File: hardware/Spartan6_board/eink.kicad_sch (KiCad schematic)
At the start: 15 parts, among them J3 FH12-40S-0.5SH, J6 DF12NB(3.0)-30DS-0.5V(51), J7 DF12NB(3.0)-30DS-0.5V(51), U6 MT9700-N

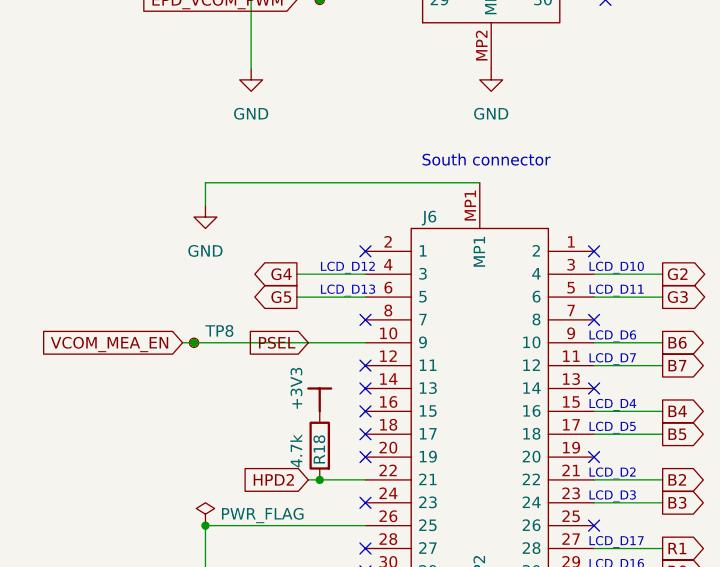
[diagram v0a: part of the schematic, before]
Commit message: fixed mixup of pins G5/G4 (3rd diff pair ODD) and DE/PCLK (3rd diff pair EVEN), now with correct polarity for diff pairs
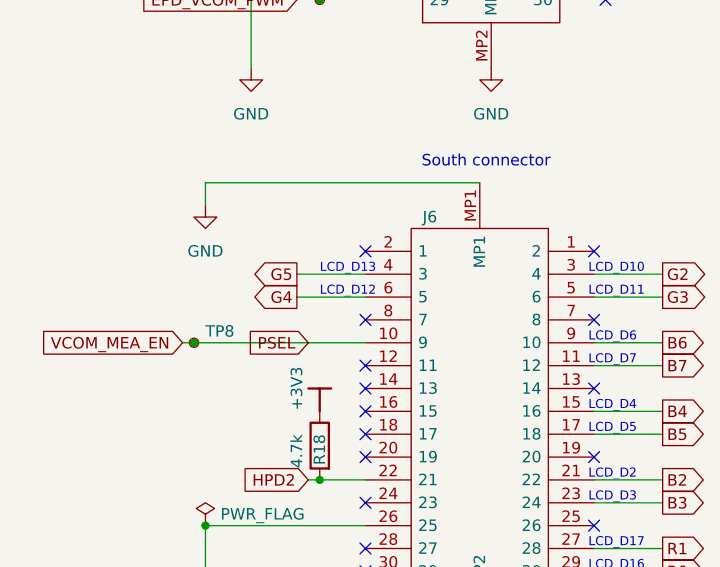
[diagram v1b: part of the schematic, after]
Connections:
- net G4: now also J6.6 (5); no longer J6.4 (3)
- net G5: now also J6.4 (3); no longer J6.6 (5)
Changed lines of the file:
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@@
+	(wire
+		(pts
+			(xy 31.75 142.24) (xy 39.37 142.24)
+		)
+		(stroke
+			(width 0.254)
+			(type default)
+		)
+	)
 	(wire
 		(pts
@@
 	(wire
 		(pts
+			(xy 129.54 118.11) (xy 129.54 119.38)
+		)
+		(stroke
+			(width 0)
+			(type default)
+		)
+	)
+	(wire
+		(pts
+			(xy 40.64 88.9) (xy 33.02 88.9)
+		)
+		(stroke
+			(width 0.254)
+			(type default)
+		)
+	)
+	(wire
+		(pts
+			(xy 33.02 91.44) (xy 40.64 91.44)
+		)
+		(stroke
+			(width 0.254)
+			(type default)
+		)
+	)
+	(wire
+		(pts
+			(xy 53.34 68.58) (xy 22.86 68.58)
+		)
+		(stroke
+			(width 0.254)
+			(type default)
+		)
+	)
+	(wire
+		(pts
+			(xy 119.38 151.13) (xy 119.38 153.67)
+		)
+		(stroke
+			(width 0)
+			(type default)
+		)
+	)
+	(wire
+		(pts
 			(xy 31.75 144.78) (xy 39.37 144.78)
 		)
@@
 	(wire
 		(pts
-			(xy 129.54 118.11) (xy 129.54 119.38)
-		)
-		(stroke
-			(width 0)
-			(type default)
-		)
-	)
-	(wire
-		(pts
-			(xy 40.64 88.9) (xy 33.02 88.9)
-		)
-		(stroke
-			(width 0.254)
-			(type default)
-		)
-	)
-	(wire
-		(pts
-			(xy 33.02 91.44) (xy 40.64 91.44)
-		)
-		(stroke
-			(width 0.254)
-			(type default)
-		)
-	)
-	(wire
-		(pts
-			(xy 53.34 68.58) (xy 22.86 68.58)
-		)
-		(stroke
-			(width 0.254)
-			(type default)
-		)
-	)
-	(wire
-		(pts
-			(xy 119.38 151.13) (xy 119.38 153.67)
-		)
-		(stroke
-			(width 0)
-			(type default)
-		)
-	)
-	(wire
-		(pts
 			(xy 107.95 140.97) (xy 109.22 140.97)
 		)
@@
 		(stroke
 			(width 0)
-			(type default)
-		)
-	)
-	(wire
-		(pts
-			(xy 31.75 142.24) (xy 39.37 142.24)
-		)
-		(stroke
-			(width 0.254)
 			(type default)
 		)
@@
 		)
 	)
-	(text "LCD_D13"
-		(exclude_from_sim no)
-		(at 34.29 144.78 0)
-		(effects
-			(font
-				(size 1 1)
-			)
-			(justify left bottom)
-		)
-	)
 	(text "LCD_D11"
 		(exclude_from_sim no)
@@
 		)
 	)
+	(text "LCD_D13"
+		(exclude_from_sim no)
+		(at 34.29 142.24 0)
+		(effects
+			(font
+				(size 1 1)
+			)
+			(justify left bottom)
+		)
+	)
 	(text "LCD_D18"
 		(exclude_from_sim no)
@@
 		)
 	)
-	(text "LCD_D12"
-		(exclude_from_sim no)
-		(at 34.29 142.24 0)
-		(effects
-			(font
-				(size 1 1)
-			)
-			(justify left bottom)
-		)
-	)
 	(text "LCD_D1"
 		(exclude_from_sim no)
@@
 		)
 	)
+	(text "LCD_D12"
+		(exclude_from_sim no)
+		(at 34.29 144.78 0)
+		(effects
+			(font
+				(size 1 1)
+			)
+			(justify left bottom)
+		)
+	)
 	(text "LCD_D9"
 		(exclude_from_sim no)
@@
 		)
 	)
+	(global_label "G5"
+		(shape output)
+		(at 31.75 142.24 180)
+		(fields_autoplaced yes)
+		(effects
+			(font
+				(size 1.27 1.27)
+			)
+			(justify right)
+		)
+		(property "Intersheetrefs" "${INTERSHEET_REFS}"
+			(at 26.2853 142.24 0)
+			(effects
+				(font
+					(size 1.27 1.27)
+				)
+				(justify right)
+				(hide yes)
+			)
+		)
+	)
 	(global_label "G1"
 		(shape output)
@@
 		(property "Intersheetrefs" "${INTERSHEET_REFS}"
 			(at 102.4853 120.65 0)
-			(effects
-				(font
-					(size 1.27 1.27)
-				)
-				(justify right)
-				(hide yes)
-			)
-		)
-	)
-	(global_label "G5"
-		(shape output)
-		(at 31.75 144.78 180)
-		(fields_autoplaced yes)
-		(effects
-			(font
-				(size 1.27 1.27)
-			)
-			(justify right)
-		)
-		(property "Intersheetrefs" "${INTERSHEET_REFS}"
-			(at 26.2853 144.78 0)
 			(effects
 				(font
@@
 		)
 	)
+	(global_label "G4"
+		(shape output)
+		(at 31.75 144.78 180)
+		(fields_autoplaced yes)
+		(effects
+			(font
+				(size 1.27 1.27)
+			)
+			(justify right)
+		)
+		(property "Intersheetrefs" "${INTERSHEET_REFS}"
+			(at 26.2853 144.78 0)
+			(effects
+				(font
+					(size 1.27 1.27)
+				)
+				(justify right)
+				(hide yes)
+			)
+		)
+	)
 	(global_label "G6"
 		(shape output)
@@
 			(effects
 				(font
-					(size 1.27 1.27)
-				)
-				(justify right)
-				(hide yes)
-			)
-		)
-	)
-	(global_label "G4"
-		(shape output)
-		(at 31.75 142.24 180)
-		(fields_autoplaced yes)
-		(effects
-			(font
-				(size 1.27 1.27)
-			)
-			(justify right)
-		)
-		(property "Intersheetrefs" "${INTERSHEET_REFS}"
-			(at 26.2853 142.24 0)
-			(effects
-				(font

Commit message: change DVI FPC pinout to match DVI connector (G-S-S-G), and FPGA device from XC6SLX16-FTG256 to XC6SLX25-3FTG256C
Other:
- title: Caster EPDC -> Spartan 6 FPGA board
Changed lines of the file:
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@@
 	(paper "A4")
 	(title_block
-		(title "Caster EPDC")
-		(date "2022-07-03")
-		(rev "R0.4")
+		(title "Spartan 6 FPGA board")
+		(date "2026-09-17")
+		(rev "R0.1")
 		(company "Copyright 2022 Modos / Engineer: Wenting Zhang")
 	)

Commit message: review and update manufacturing constraints (via size, etc.)
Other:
- company: Copyright 2022 Modos / Engineer: Wenting Zhang -> (C) 2025-2026 Victor Suarez Rovere <suarezvictor@gmail.com>
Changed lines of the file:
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@@
 	(title_block
 		(title "Spartan 6 FPGA board")
-		(date "2026-09-17")
+		(date "2026-09-18")
 		(rev "R0.1")
-		(company "Copyright 2022 Modos / Engineer: Wenting Zhang")
+		(company "(C) 2025-2026 Victor Suarez Rovere <suarezvictor@gmail.com>")
+		(comment 1 "Copyright 2023 Modos / Engineer: Wenting Zhang")
 	)
 	(junction

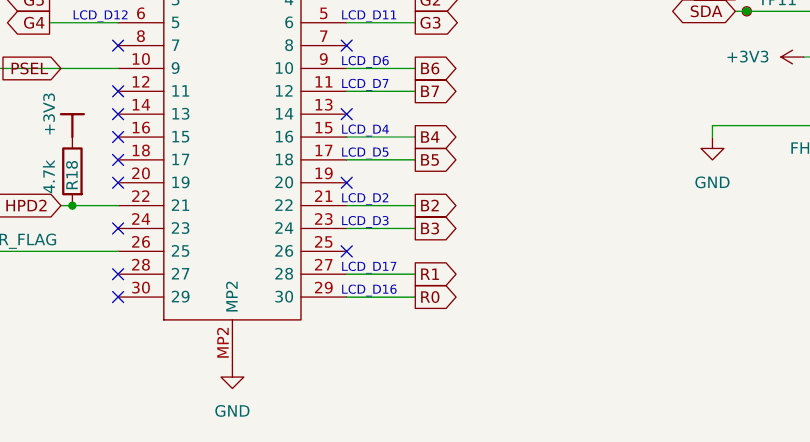
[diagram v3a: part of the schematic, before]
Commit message: fix R0/R1 mixup
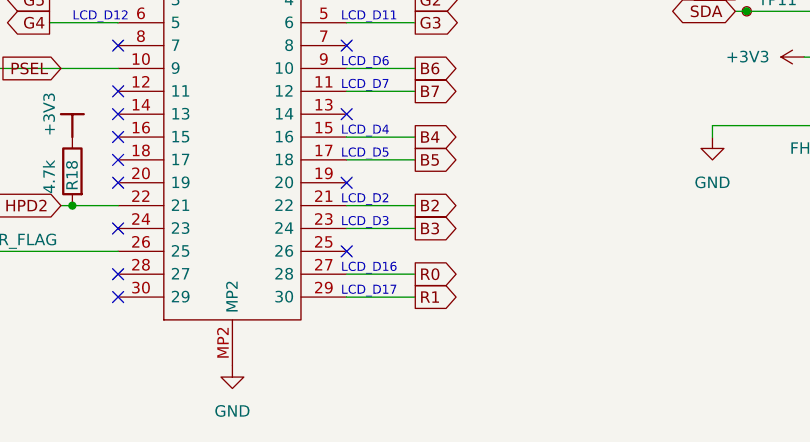
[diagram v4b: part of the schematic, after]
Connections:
- net R0: now also J6.27 (28); no longer J6.29 (30)
- net R1: now also J6.29 (30); no longer J6.27 (28)
